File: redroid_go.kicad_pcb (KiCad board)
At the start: 2 copper layers, 70 x 95 mm, 100 parts, among them J1 USB4105-GF-A, J2 5051101892, J3 Conn_01x02_Pin, J4 Conn_01x10_Pin, Q1 UMH3N, Q2 PMOS, Q3 UMH3N, SW1 UP, SW10 A, SW11 SW_SPDT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

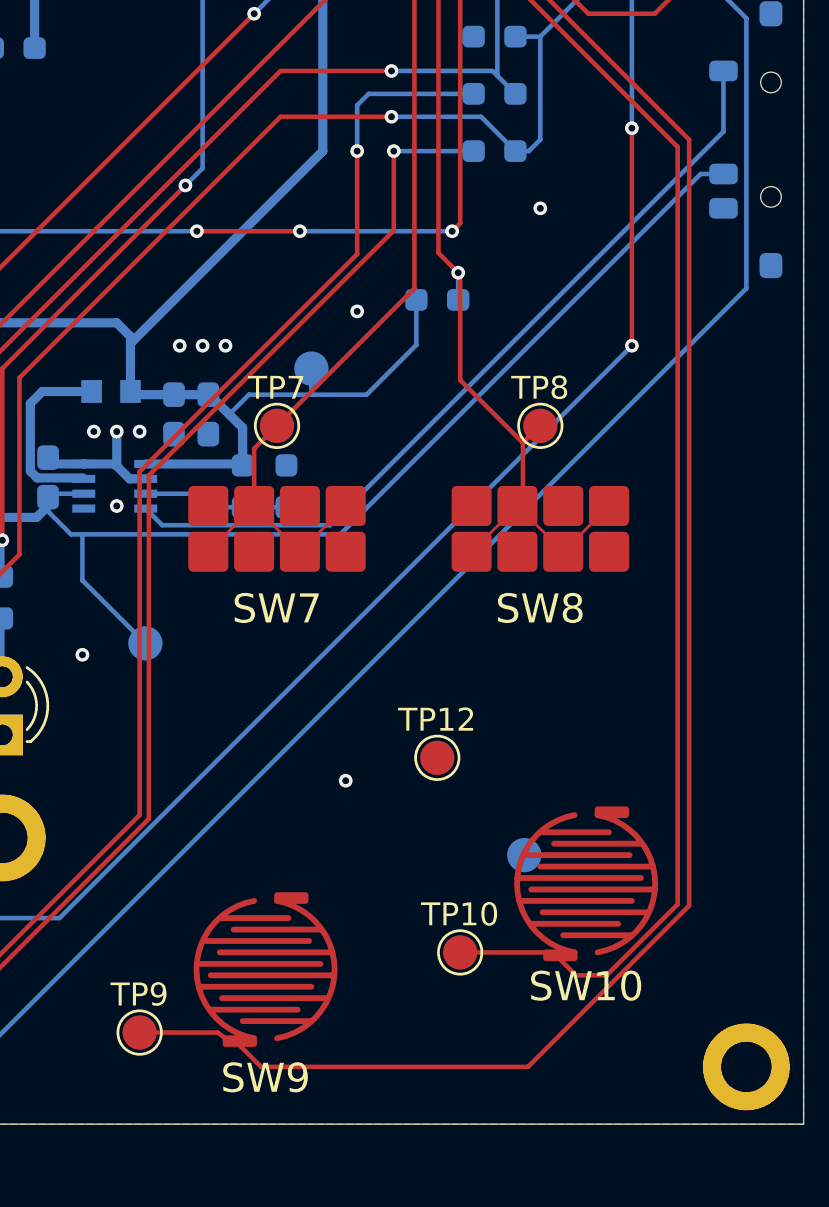
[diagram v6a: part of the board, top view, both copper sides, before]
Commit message: Improve A and B buttons pads
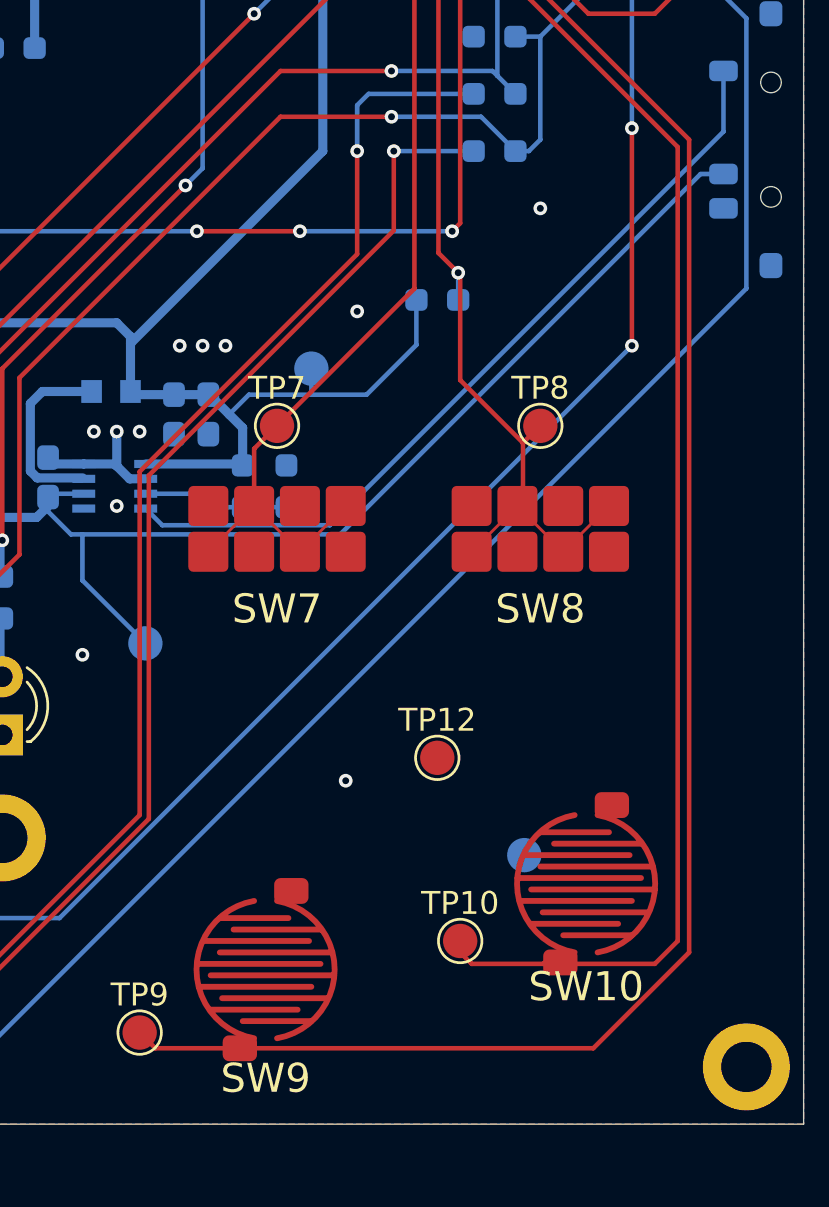
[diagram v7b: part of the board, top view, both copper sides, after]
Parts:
- moved TP10 0.50 mm to (183.5, 120.5)
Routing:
- net IO33: track 90.6 -> 92.1 mm
- net IO32: track 75.7 -> 76.6 mm
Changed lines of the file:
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@@
 		)
 		(pad "P$ACTIVE" smd roundrect
-			(at 1.125 -3.125 180)
-			(size 1.5 0.508)
+			(at 1.125 -3.4355 180)
+			(size 1.5 1.129)
 			(layers "F.Cu")
 			(roundrect_rratio 0.25)
@@
 		)
 		(pad "P$GND" smd roundrect
-			(at -1.125 3.125)
-			(size 1.5 0.508)
+			(at -1.125 3.4355)
+			(size 1.5 1.129)
 			(layers "F.Cu")
 			(roundrect_rratio 0.25)
@@
 		)
 		(pad "P$ACTIVE" smd roundrect
-			(at 1.125 -3.125 180)
-			(size 1.5 0.508)
+			(at 1.125 -3.4355 180)
+			(size 1.5 1.129)
 			(layers "F.Cu")
 			(roundrect_rratio 0.25)
@@
 		)
 		(pad "P$GND" smd roundrect
-			(at -1.125 3.125)
-			(size 1.5 0.508)
+			(at -1.125 3.4355)
+			(size 1.5 1.129)
 			(layers "F.Cu")
 			(roundrect_rratio 0.25)
@@
 	(footprint "TestPoint:TestPoint_Pad_D1.5mm"
 		(layer "F.Cu")
-		(at 183.5 121)
+		(at 183.5 120.5)
 		(descr "SMD pad as test Point, diameter 1.5mm")
 		(tags "test point SMD pad")
@@
 	)
 	(segment
-		(start 169.5 124.5)
-		(end 172.898863 124.5)
+		(start 190 62)
+		(end 188.5 63.5)
+		(width 0.2)
+		(layer "F.Cu")
+		(net 63)
+	)
+	(segment
+		(start 187 79)
+		(end 193.5 85.5)
 		(width 0.2)
 		(layer "F.Cu")
@@
 	)
 	(segment
-		(start 193.5 118.96018)
-		(end 186.46018 126)
+		(start 170.1855 125.1855)
+		(end 173.875 125.1855)
 		(width 0.2)
 		(layer "F.Cu")
@@
 	)
 	(segment
-		(start 174.806193 126)
-		(end 173.817642 125.011449)
+		(start 193.5 121)
+		(end 189.3145 125.1855)
 		(width 0.2)
 		(layer "F.Cu")
@@
 	)
 	(segment
-		(start 173.163527 124.689483)
-		(end 173.502815 124.879107)
+		(start 188.5 63.5)
+		(end 188.5 71.565686)
 		(width 0.2)
 		(layer "F.Cu")
@@
 	)
 	(segment
-		(start 186.46018 126)
-		(end 174.806193 126)
+		(start 173.875 125.1855)
+		(end 173.809208 125.1855)
 		(width 0.2)
 		(layer "F.Cu")
@@
 	)
 	(segment
-		(start 193.5 85.5)
-		(end 193.5 118.96018)
+		(start 187 73.065686)
+		(end 187 79)
 		(width 0.2)
 		(layer "F.Cu")
@@
 	)
 	(segment
-		(start 187 79)
-		(end 193.5 85.5)
+		(start 173.991693 125.1855)
+		(end 173.817642 125.011449)
 		(width 0.2)
 		(layer "F.Cu")
@@
 	)
 	(segment
-		(start 190 62)
-		(end 188.5 63.5)
+		(start 193.5 85.5)
+		(end 193.5 121)
 		(width 0.2)
 		(layer "F.Cu")
@@
 	)
 	(segment
-		(start 188.5 63.5)
-		(end 188.5 71.565686)
+		(start 189.3145 125.1855)
+		(end 173.991693 125.1855)
 		(width 0.2)
 		(layer "F.Cu")
@@
 	)
 	(segment
-		(start 172.898863 124.5)
-		(end 173.163527 124.689483)
+		(start 169.5 124.5)
+		(end 170.1855 125.1855)
 		(width 0.2)
 		(layer "F.Cu")
@@
 	)
 	(segment
-		(start 187 73.065686)
-		(end 187 79)
+		(start 173.809208 125.1855)
+		(end 173.502815 124.879107)
 		(width 0.2)
 		(layer "F.Cu")
@@
 	)
 	(segment
-		(start 193 85.820126)
-		(end 193 118.894494)
+		(start 188 71.5)
+		(end 186.5 73)
 		(width 0.2)
 		(layer "F.Cu")
@@
 	)
 	(segment
-		(start 188 63)
-		(end 188 71.5)
+		(start 187.817642 121.261449)
+		(end 187.502815 121.129107)
 		(width 0.2)
 		(layer "F.Cu")
@@
 	)
 	(segment
-		(start 188.556193 122)
-		(end 187.817642 121.261449)
+		(start 187.502815 121.129107)
+		(end 187.131922 121.5)
+		(width 0.2)
+		(layer "F.Cu")
+		(net 64)
+	)
+	(segment
+		(start 192 121.5)
+		(end 188.056193 121.5)
 		(width 0.2)
 		(layer "F.Cu")
@@
 	)
 	(segment
-		(start 186.5 73)
-		(end 186.5 79.320126)
+		(start 184 121.5)
+		(end 183.5 121)
 		(width 0.2)
 		(layer "F.Cu")
@@
 	)
 	(segment
-		(start 190 61)
-		(end 188 63)
+		(start 188 63)
+		(end 188 71.5)
 		(width 0.2)
 		(layer "F.Cu")
@@
 	)
 	(segment
-		(start 187.817642 121.261449)
-		(end 187.502815 121.129107)
+		(start 186.5 73)
+		(end 186.5 79.320126)
 		(width 0.2)
 		(layer "F.Cu")
@@
 	)
 	(segment
-		(start 187.271808 121)
-		(end 183.5 121)
+		(start 190 61)
+		(end 188 63)
 		(width 0.2)
 		(layer "F.Cu")
@@
 	)
 	(segment
-		(start 193 118.894494)
-		(end 189.894494 122)
+		(start 193 120.5)
+		(end 192 121.5)
 		(width 0.2)
 		(layer "F.Cu")
@@
 	)
 	(segment
-		(start 189.894494 122)
-		(end 188.556193 122)
+		(start 188.056193 121.5)
+		(end 187.817642 121.261449)
 		(width 0.2)
 		(layer "F.Cu")
@@
 	)
 	(segment
-		(start 188 71.5)
-		(end 186.5 73)
+		(start 187.131922 121.5)
+		(end 184 121.5)
 		(width 0.2)
 		(layer "F.Cu")
@@
 	)
 	(segment
-		(start 187.502815 121.129107)
-		(end 187.271808 121)
+		(start 193 85.820126)
+		(end 193 120.5)
 		(width 0.2)
 		(layer "F.Cu")

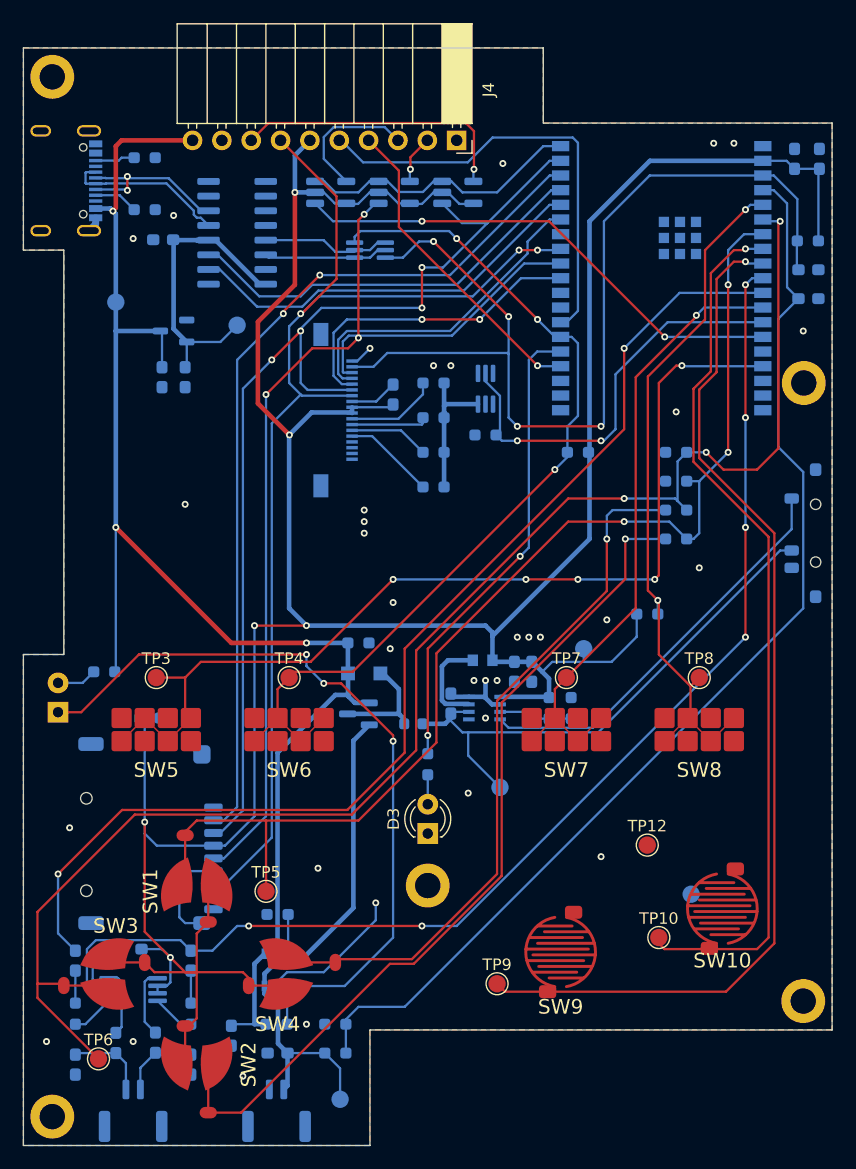
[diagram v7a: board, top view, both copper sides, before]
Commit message: Relocate components
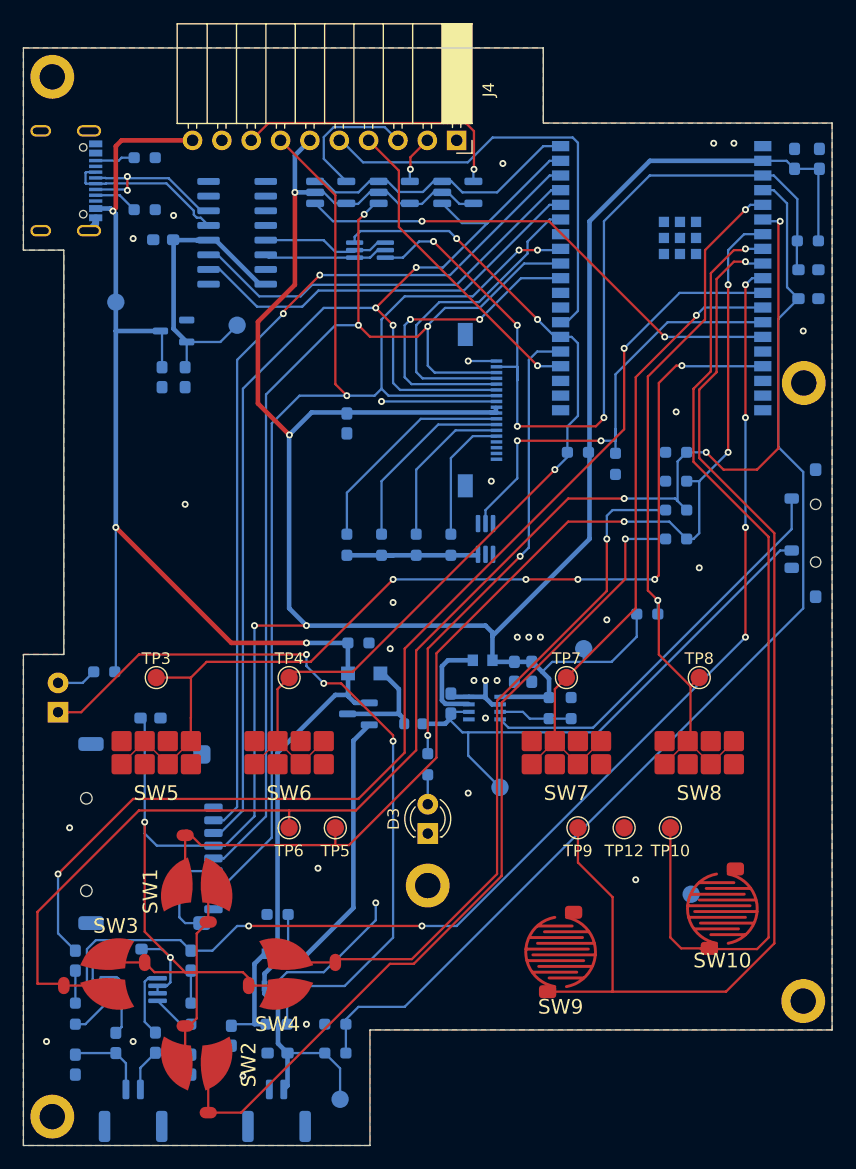
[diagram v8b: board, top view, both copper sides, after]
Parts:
- moved TP6 25.9 mm to (151.5, 111.0)
- moved R24 15.9 mm to (156.5, 86.5), turned to 90 degrees
- moved TP9 15.2 mm to (176.5, 111.0)
- moved Q3 13.0 mm to (168.5, 86.0)
- moved J2 12.5 mm to (167.0, 74.8)
- moved R25 11.9 mm to (159.5, 86.5), turned to 90 degrees
- moved R20 11.5 mm to (179.8, 79.5), turned to -90 degrees
- moved TP10 9.55 mm to (184.5, 111.0)
- moved R19 8.14 mm to (162.5, 86.5), turned to 90 degrees
- moved TP5 8.14 mm to (155.5, 111.0)
- moved R26 5.22 mm to (165.5, 86.5), turned to 90 degrees
- moved C10 4.72 mm to (156.5, 76.0), turned to -90 degrees
- moved TP12 2.50 mm to (180.5, 111.0)
- moved SW5 2.00 mm to (140.0, 104.5)
- moved SW6 2.00 mm to (151.5, 104.5)
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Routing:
- net Net-(J2-LEDK1): track 7.49 -> 19.2 mm
- net RESET: track 88.2 -> 76.8 mm
- net MISO: track 101.5 -> 112.0 mm
- net Net-(J2-LEDK2): track 6.18 -> 16.6 mm
- net IO33: track 92.1 -> 102.2 mm
- net IO32: track 76.6 -> 86.0 mm
- net P3V3: track 266.8 -> 275.9 mm
- net IO34: track 128.6 -> 120.9 mm
- net Net-(J2-LEDK3): track 6.92 -> 13.9 mm
- net GND: track 66.3 -> 72.6 mm, vias 34 -> 31
- net MOSI: track 91.0 -> 95.9 mm, vias 4 -> 3
- net SCK: track 90.2 -> 94.7 mm
- net Net-(J2-LEDK4): track 7.96 -> 11.3 mm
- net IO14: track 36.3 -> 39.3 mm
- net IO35: track 97.3 -> 94.5 mm
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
